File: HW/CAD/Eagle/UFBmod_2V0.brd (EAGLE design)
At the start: 98.4 x 89.5 mm, 193 parts, among them T0551 MMBT2222, U0501 MIDAS_MCCOG21605B6W-FPTLWI, U0601 MAX5217, U0701 AT86RF215-ZU, U0711 ASVTX-13-D-26.000MHZ-I05-T, U0811 PE4259, U0821 RFX1010, U0881 B39871B3440U410, U0911 FT232HL, U1101 TPS53353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

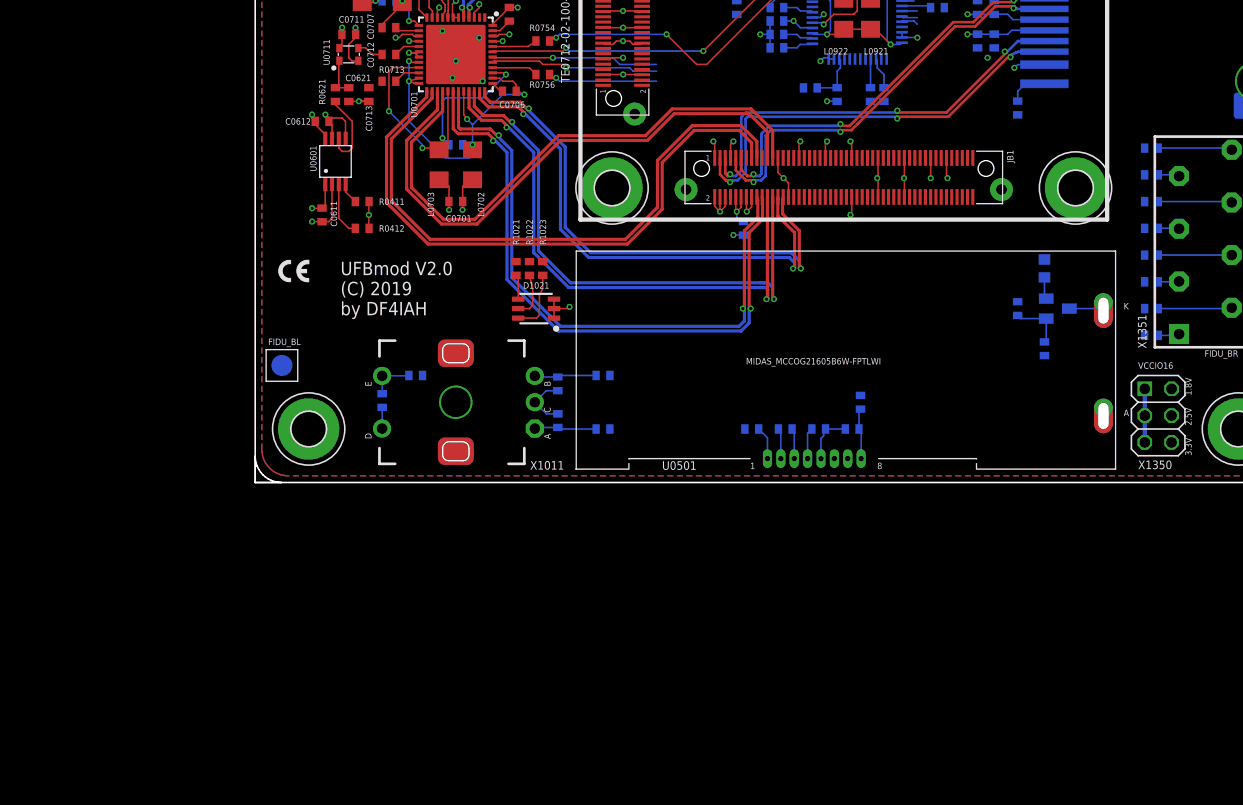
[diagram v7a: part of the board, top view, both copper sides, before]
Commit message: HW - CAD/Eagle - update FPGA assignments
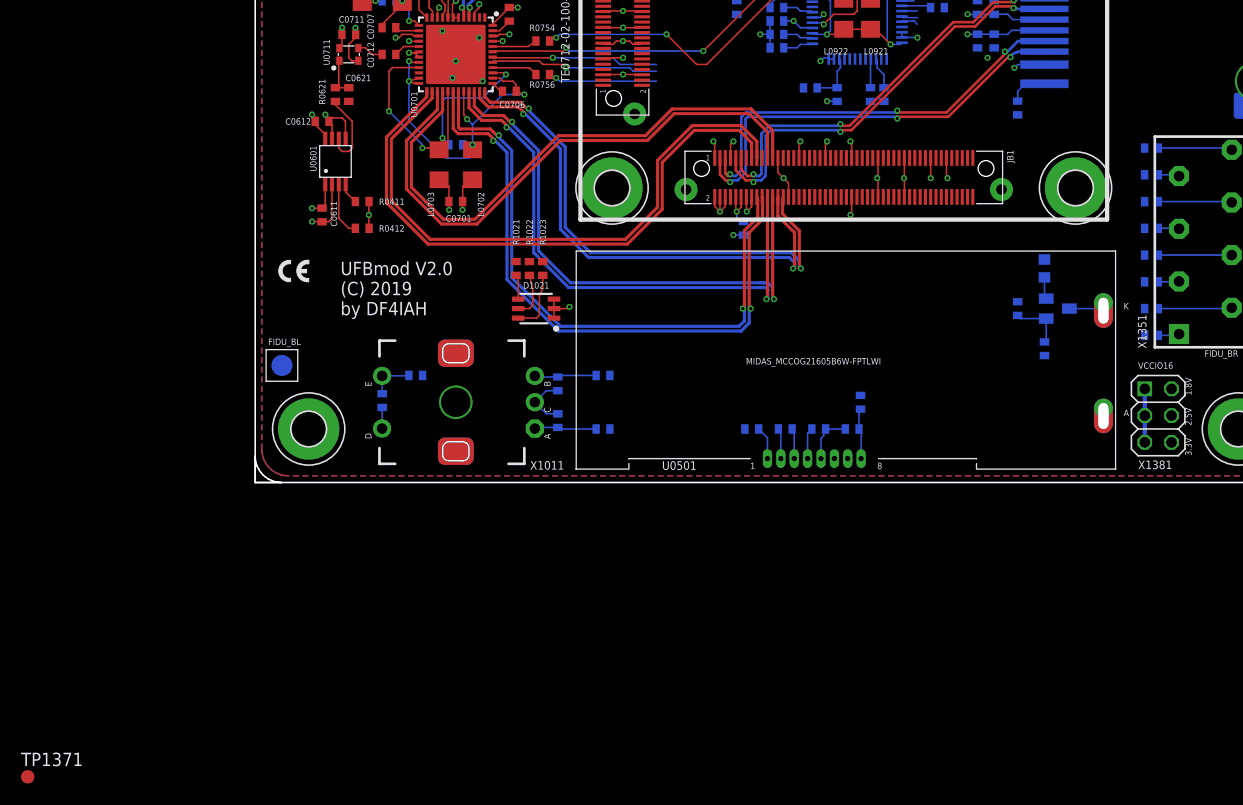
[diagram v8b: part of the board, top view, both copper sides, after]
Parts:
- removed C0713: 56pF, df4iah_rcl:C0402
- removed R0713: 100R, df4iah_rcl:R0402
- added TP1371: TPB1,27, df4iah_connector:B1,27
- renumbered C1350 to C1381, X1350 to X1381
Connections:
- net FPGA_I2C_SCL renamed BOARD_SCL
- net FPGA_I2C_SDA renamed BOARD_SDA
- net FPGA_LCD_NRST renamed BOARD_LCD_RESETN
- removed net FPGA_TRX_CLKO: C0713.1, JB1.76, R0713.1
- removed net TRX_CLKO: R0713.2, U0701.22
- new net INIT_CALIB_COMPLETE: TP1371.TP
- net FPGA_LCD_BL_PWM: no longer JB1.84
- net FPGA_LED_RGB_BLUE: no longer JB1.36
- net FPGA_LED_RGB_GREEN: no longer JB1.34
- net FPGA_LED_RGB_RED: no longer JB1.32
- net GND: no longer C0713.2
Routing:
- net GND: track 228.8 -> 225.9 mm, vias 80 -> 79
- net TRX_CLKO: track 2.53 -> 0.00 mm
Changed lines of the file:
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@@
 <attribute name="VALUE" x="17.78" y="25.0825" size="0.6096" layer="27" font="vector" ratio="10"/>
 </element>
-<element name="R0713" library="df4iah_rcl" package="R0402" value="100R" x="12.7" y="38.1" smashed="yes">
-<attribute name="NAME" x="11.7475" y="38.89375" size="0.6096" layer="25" font="vector" ratio="10"/>
-<attribute name="VALUE" x="11.1125" y="36.5125" size="0.6096" layer="27" font="vector" ratio="10"/>
-</element>
-<element name="C0713" library="df4iah_rcl" package="C0402" value="56pF" x="10.795" y="36.83" smashed="yes" rot="R270">
-<attribute name="NAME" x="11.1125" y="33.3375" size="0.6096" layer="25" font="vector" ratio="10" rot="R90"/>
-<attribute name="VALUE" x="9.2075" y="38.1" size="0.6096" layer="27" font="vector" ratio="10" rot="R270"/>
-</element>
 <element name="U0711" library="df4iah_osc" package="ASVTX-13" value="ASVTX-13-D-26.000MHZ-I05-T" x="8.89" y="40.64" smashed="yes">
 <attribute name="NAME" x="7.090146875" y="39.6013" size="0.6096" layer="25" font="vector" rot="R90"/>
@@
 <attribute name="VALUE" x="83.5025" y="71.4375" size="0.6096" layer="28" font="vector" ratio="10" rot="MR180"/>
 </element>
-<element name="X1350" library="df4iah_connector" package="2X03" value="" x="85.725" y="6.35" locked="yes" smashed="yes" rot="R270">
+<element name="X1381" library="df4iah_connector" package="2X03" value="" x="85.725" y="6.35" locked="yes" smashed="yes" rot="R270">
 <attribute name="NAME" x="83.82" y="1.27" size="0.8128" layer="25" font="vector" ratio="20"/>
 <attribute name="VALUE" x="81.28" y="10.16" size="1.27" layer="27" rot="R270"/>
 </element>
-<element name="C1350" library="df4iah_rcl" package="C0402" value="100nF" x="46.355" y="24.13" smashed="yes" rot="MR90">
+<element name="C1381" library="df4iah_rcl" package="C0402" value="100nF" x="46.355" y="24.13" smashed="yes" rot="MR90">
 <attribute name="NAME" x="47.3075" y="22.86" size="0.6096" layer="26" font="vector" ratio="10" rot="MR90"/>
 <attribute name="VALUE" x="44.7675" y="22.86" size="0.6096" layer="28" font="vector" ratio="10" rot="MR90"/>
@@
 <attribute name="VALUE" x="25.7175" y="40.3225" size="0.6096" layer="27" font="vector" ratio="10"/>
 </element>
+<element name="TP1371" library="df4iah_connector" package="B1,27" value="TPB1,27" x="-21.59" y="-27.94">
+<attribute name="TP_SIGNAL_NAME" value="" x="-21.59" y="-27.94" size="0.6096" layer="27" ratio="20" display="off"/>
+</element>
 </elements>
 <signals>
@@
 <contactref element="L0702" pad="1"/>
 <contactref element="C0701" pad="2"/>
-<contactref element="C0713" pad="2"/>
 <contactref element="U0711" pad="2"/>
 <contactref element="C0711" pad="2"/>
@@
 <wire x1="5.7" y1="34.29" x2="5.3975" y2="34.5925" width="0.1524" layer="1"/>
 <wire x1="5.3975" y1="34.5925" x2="5.3975" y2="34.925" width="0.1524" layer="1"/>
-<wire x1="10.795" y1="36.18" x2="8.89" y2="36.18" width="0.1524" layer="1"/>
-<via x="9.8425" y="36.195" extent="1-16" drill="0.3"/>
-<wire x1="10.795" y1="36.18" x2="10.78" y2="36.195" width="0.1524" layer="1"/>
-<wire x1="10.78" y1="36.195" x2="9.8425" y2="36.195" width="0.1524" layer="1"/>
 <via x="9.525" y="43.18" extent="1-16" drill="0.3"/>
 <wire x1="9.54" y1="42.545" x2="9.525" y2="42.56" width="0.1524" layer="1"/>
@@
 <contactref element="X1331" pad="11"/>
 <contactref element="X1331" pad="13"/>
-<contactref element="C1350" pad="1"/>
+<contactref element="C1381" pad="1"/>
 <wire x1="54.14875" y1="5.08" x2="53.975" y2="4.90625" width="0.1524" layer="16"/>
 <wire x1="53.975" y1="4.90625" x2="53.975" y2="4.445" width="0.1524" layer="16"/>
@@
 <wire x1="26.035" y1="77.47" x2="26.02" y2="77.47" width="0" layer="19" extent="1-1"/>
 <wire x1="9.525" y1="43.18" x2="13.97" y2="48.412" width="0" layer="19" extent="1-1"/>
-<wire x1="9.8425" y1="36.195" x2="9.755" y2="40.005" width="0" layer="19" extent="1-1"/>
+<wire x1="8.89" y1="36.18" x2="9.2075" y2="40.005" width="0" layer="19" extent="1-1"/>
 <wire x1="5.3975" y1="34.925" x2="8.89" y2="36.18" width="0" layer="19" extent="1-1"/>
 <wire x1="7.295" y1="28.33" x2="6.645" y2="32.63" width="0" layer="19" extent="1-1"/>
@@
 <wire x1="28.37" y1="17.41" x2="33.88" y2="27.96" width="0" layer="19" extent="1-1"/>
 <wire x1="28.73375" y1="8.71625" x2="28.37" y2="15.61" width="0" layer="19" extent="1-16"/>
-<wire x1="19.7" y1="28.1205" x2="10.795" y2="36.18" width="0" layer="19" extent="1-1"/>
+<wire x1="19.685" y1="25.87625" x2="28.37" y2="17.41" width="0" layer="19" extent="1-1"/>
 <wire x1="12.05" y1="7.11375" x2="26.55" y2="7.62" width="0" layer="19" extent="16-16"/>
 <wire x1="5.08" y1="5.08" x2="12.05" y2="5.12" width="0" layer="19" extent="1-1"/>
@@
 <wire x1="26.655" y1="41.91" x2="25.905" y2="41.39" width="0.1524" layer="1"/>
 </signal>
-<signal name="FPGA_TRX_CLKO">
-<contactref element="R0713" pad="1"/>
-<contactref element="C0713" pad="1"/>
-<contactref element="JB1" pad="76"/>
-<wire x1="12.05" y1="38.1" x2="62.13" y2="27.11" width="0" layer="19" extent="1-1"/>
-<wire x1="10.795" y1="37.48" x2="12.05" y2="38.1" width="0" layer="19" extent="1-1"/>
-</signal>
-<signal name="TRX_CLKO">
-<contactref element="U0701" pad="22"/>
-<contactref element="R0713" pad="2"/>
-<wire x1="15.55" y1="38.89" x2="14.14" y2="38.89" width="0.1524" layer="1"/>
-<wire x1="14.14" y1="38.89" x2="13.35" y2="38.1" width="0.1524" layer="1"/>
-</signal>
 <signal name="TRX_DVSS">
 <contactref element="L0702" pad="2"/>
@@
 <wire x1="7.62" y1="35.8775" x2="7.62" y2="36.18" width="0.1524" layer="1"/>
 </signal>
-<signal name="FPGA_I2C_SCL">
+<signal name="BOARD_SCL">
 <contactref element="R0412" pad="1"/>
 <contactref element="U0601" pad="3"/>
@@
 <wire x1="9.51" y1="24.13" x2="56.255" y2="2.27" width="0" layer="19" extent="1-1"/>
 </signal>
-<signal name="FPGA_I2C_SDA">
+<signal name="BOARD_SDA">
 <contactref element="R0411" pad="1"/>
 <contactref element="U0601" pad="4"/>
@@
 <signal name="FPGA_LED_RGB_GREEN">
 <contactref element="R1022" pad="2"/>
-<contactref element="JB1" pad="34"/>
-<wire x1="26.035" y1="20.97" x2="51.63" y2="27.11" width="0" layer="19" extent="1-1"/>
 </signal>
 <signal name="FPGA_LED_RGB_BLUE">
 <contactref element="R1023" pad="2"/>
-<contactref element="JB1" pad="36"/>
-<wire x1="27.305" y1="20.97" x2="52.13" y2="27.11" width="0" layer="19" extent="1-1"/>
 </signal>
 <signal name="LED_RGB_RED">
@@
 <signal name="FPGA_LED_RGB_RED">
 <contactref element="R1021" pad="2"/>
-<contactref element="JB1" pad="32"/>
-<wire x1="24.765" y1="20.97" x2="51.13" y2="27.11" width="0" layer="19" extent="1-1"/>
 </signal>
 <signal name="ROT_P">
@@
 <signal name="FPGA_LCD_BL_PWM">
 <contactref element="R0552" pad="2"/>
-<contactref element="JB1" pad="84"/>
-<wire x1="72.39" y1="17.16" x2="64.13" y2="27.11" width="0" layer="19" extent="1-16"/>
 </signal>
 <signal name="+5V_USB">
@@
 <wire x1="71.12" y1="87.63" x2="71.12" y2="86.375" width="0.1524" layer="1"/>
 </signal>
-<signal name="FPGA_LCD_NRST">
-<contactref element="R0532" pad="1"/>
-</signal>
 <signal name="FPGA_ROT_I">
 <contactref element="R1011" pad="2"/>
@@
 <contactref element="C1221" pad="1"/>
 <contactref element="U1211" pad="5"/>
-<contactref element="X1350" pad="4"/>
+<contactref element="X1381" pad="4"/>
 <wire x1="41.85375" y1="52.705" x2="42.70375" y2="55.07125" width="0" layer="19" extent="16-16"/>
 <wire x1="41.11625" y1="50.53" x2="41.85375" y2="52.705" width="0" layer="19" extent="16-16"/>
@@
 <contactref element="JB2" pad="10"/>
 <contactref element="R1211" pad="1"/>
-<contactref element="X1350" pad="6"/>
+<contactref element="X1381" pad="6"/>
 <wire x1="45.63" y1="62.81" x2="46.13" y2="62.81" width="0" layer="19" extent="1-1"/>
 <wire x1="45.63" y1="59.11" x2="45.63" y2="62.81" width="0" layer="19" extent="1-1"/>
@@
 <contactref element="JB1" pad="40"/>
 <contactref element="R0202" pad="1"/>
-<contactref element="X1350" pad="2"/>
+<contactref element="X1381" pad="2"/>
 <wire x1="53.13" y1="27.11" x2="44.1325" y2="55.07125" width="0" layer="19" extent="1-16"/>
 <wire x1="86.995" y1="8.89" x2="53.13" y2="27.11" width="0" layer="19" extent="1-1"/>
@@
 <contactref element="JB1" pad="10"/>
 <contactref element="JB1" pad="12"/>
-<contactref element="X1350" pad="1"/>
-<contactref element="X1350" pad="3"/>
-<contactref element="X1350" pad="5"/>
-<contactref element="C1350" pad="2"/>
+<contactref element="X1381" pad="1"/>
+<contactref element="X1381" pad="3"/>
+<contactref element="X1381" pad="5"/>
+<contactref element="C1381" pad="2"/>
 <wire x1="84.455" y1="8.89" x2="84.455" y2="6.35" width="0.4064" layer="16"/>
 <wire x1="84.455" y1="6.35" x2="84.455" y2="3.81" width="0.4064" layer="16"/>
@@
 <wire x1="63.8175" y1="57.785" x2="64.135" y2="57.4675" width="0.1524" layer="1"/>
 </signal>
+<signal name="BOARD_LCD_RESETN">
+<contactref element="R0532" pad="1"/>
+</signal>
+<signal name="INIT_CALIB_COMPLETE">
+<contactref element="TP1371" pad="TP"/>
+</signal>
 </signals>
